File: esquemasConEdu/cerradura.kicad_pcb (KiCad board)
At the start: 2 copper layers, 87.7 x 141.8 mm, 20 parts, among them T1 BC547, T2 BC547

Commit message: corregido distancia limite tracks con borde, pads ampliados y pines EDU con numeros pares
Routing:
- net GND: track 150.6 -> 134.0 mm
- net /kp_c2: track 35.3 -> 38.0 mm
- net /rc522-mosi: track 43.8 -> 46.4 mm
- net +5V: track 334.9 -> 332.4 mm
- net /kp_f2: track 30.0 -> 32.2 mm
- net /rc522-sck: track 57.9 -> 56.6 mm
- net /ssd1306_sda: track 77.9 -> 76.9 mm
- net +12V: track 191.8 -> 191.0 mm
- net /ssd1306_scl: track 76.7 -> 76.0 mm

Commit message: corregido distancia limite tracks con borde, pads ampliados y pines EDU con numeros pares
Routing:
- net +3.3V: track 270.5 -> 271.8 mm
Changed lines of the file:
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@@
 			)
 		)
+		(pad "0" thru_hole circle
+			(at 0 2.54 90)
+			(size 2 2)
+			(drill 0.7)
+			(layers "*.Cu" "*.Mask")
+			(remove_unused_layers no)
+			(pinfunction "~{EN}")
+			(pintype "input")
+		)
+		(pad "0" thru_hole oval
+			(at 12.68 12.7 90)
+			(size 2 2)
+			(drill 0.7)
+			(layers "*.Cu" "*.Mask")
+			(remove_unused_layers no)
+			(pinfunction "~{EN}")
+			(pintype "input")
+		)
+		(pad "0" thru_hole oval
+			(at 12.69 15.24 90)
+			(size 2 2)
+			(drill 0.7)
+			(layers "*.Cu" "*.Mask")
+			(remove_unused_layers no)
+			(pinfunction "~{EN}")
+			(pintype "input")
+		)
+		(pad "0" thru_hole circle
+			(at 12.71 10.16 90)
+			(size 2 2)
+			(drill 0.7)
+			(layers "*.Cu" "*.Mask")
+			(remove_unused_layers no)
+			(pinfunction "~{EN}")
+			(pintype "input")
+		)
 		(pad "1" thru_hole oval
 			(at 0 0 90)
@@
 		(pad "9" thru_hole circle
 			(at 12.7 17.78 90)
-			(size 1.7 1.7)
+			(size 2 2)
 			(drill 0.7)
 			(layers "*.Cu" "*.Mask")
@@
 			)
 		)
+		(pad "0" thru_hole oval
+			(at -2.55 0)
+			(size 2 2)
+			(drill 0.7)
+			(layers "*.Cu" "*.Mask")
+			(remove_unused_layers no)
+			(pinfunction "~{EN}")
+			(pintype "input")
+		)
+		(pad "0" thru_hole circle
+			(at 12.68 5.08)
+			(size 2 2)
+			(drill 0.7)
+			(layers "*.Cu" "*.Mask")
+			(remove_unused_layers no)
+			(pinfunction "~{EN}")
+			(pintype "input")
+		)
 		(pad "1" thru_hole circle
 			(at 12.7 0 180)
@@
 	)
 	(segment
-		(start 114.216 160.784)
-		(end 114.216 122.196159)
+		(start 85.41 167.64)
+		(end 107.36 167.64)
+		(width 1)
+		(layer "B.Cu")
+		(net 1)
+	)
+	(segment
+		(start 73.19 170.26)
+		(end 73.19 165.48)
 		(width 1)
 		(layer "B.Cu")
@@
 	)
 	(segment
+		(start 80.58 162.81)
+		(end 85.41 167.64)
+		(width 1)
+		(layer "B.Cu")
+		(net 1)
+	)
+	(segment
 		(start 99.3925 85.7)
 		(end 101.88 85.7)
@@
 	)
 	(segment
-		(start 114.216 122.196159)
-		(end 112.489841 120.47)
+		(start 107.36 167.64)
+		(end 114.216 160.784)
 		(width 1)
 		(layer "B.Cu")
@@
 	)
 	(segment
-		(start 122.62 85.7)
-		(end 101.88 85.7)
+		(start 112.489841 120.47)
+		(end 109.41 120.47)
 		(width 1)
 		(layer "B.Cu")
@@
 	)
 	(segment
-		(start 79.519 163.819)
-		(end 83.34 167.64)
+		(start 73.19 165.48)
+		(end 75.86 162.81)
 		(width 1)
 		(layer "B.Cu")
@@
 	)
 	(segment
-		(start 64.19 110.15)
-		(end 62.28 112.06)
+		(start 122.62 85.7)
+		(end 101.88 85.7)
 		(width 1)
 		(layer "B.Cu")
@@
 	)
 	(segment
-		(start 107.36 167.64)
-		(end 114.216 160.784)
+		(start 64.19 110.15)
+		(end 62.28 112.06)
 		(width 1)
 		(layer "B.Cu")
@@
 	)
 	(segment
-		(start 73.19 170.26)
-		(end 73.19 166.24)
+		(start 114.216 122.196159)
+		(end 112.489841 120.47)
 		(width 1)
 		(layer "B.Cu")
@@
 	)
 	(segment
-		(start 75.611 163.819)
-		(end 79.519 163.819)
+		(start 114.216 160.784)
+		(end 114.216 122.196159)
 		(width 1)
 		(layer "B.Cu")
@@
 	)
 	(segment
-		(start 137.61 110.11)
-		(end 137.61 100.69)
+		(start 75.86 162.81)
+		(end 80.58 162.81)
 		(width 1)
 		(layer "B.Cu")
@@
 	)
 	(segment
-		(start 112.489841 120.47)
-		(end 109.41 120.47)
+		(start 137.61 110.11)
+		(end 137.61 100.69)
 		(width 1)
 		(layer "B.Cu")
@@
 	)
 	(segment
-		(start 83.34 167.64)
-		(end 107.36 167.64)
-		(width 1)
-		(layer "B.Cu")
-		(net 1)
-	)
-	(segment
-		(start 73.19 166.24)
-		(end 75.611 163.819)
-		(width 1)
-		(layer "B.Cu")
-		(net 1)
-	)
-	(segment
 		(start 74.15 115.22)
 		(end 69.03 115.22)
@@
 	)
 	(segment
-		(start 78.42 166.32)
-		(end 78.42 166.5)
+		(start 80.19 166.32)
+		(end 83.35 169.48)
 		(width 1)
 		(layer "B.Cu")
@@
 	)
 	(segment
-		(start 78.42 166.5)
-		(end 82.18 170.26)
+		(start 78.42 166.32)
+		(end 80.19 166.32)
 		(width 1)
 		(layer "B.Cu")
@@
 	)
 	(segment
-		(start 82.18 170.26)
+		(start 83.35 169.48)
 		(end 83.35 170.26)
 		(width 1)
@@
 	)
 	(segment
-		(start 112.215 123.025)
-		(end 109.3 123.025)
+		(start 112.18 157.45)
+		(end 112.18 123.06)
 		(width 1)
 		(layer "B.Cu")
@@
 	)
 	(segment
-		(start 112.18 123.06)
-		(end 112.215 123.025)
+		(start 103.991 165.639)
+		(end 112.18 157.45)
 		(width 1)
 		(layer "B.Cu")
@@
 	)
 	(segment
-		(start 103.991 165.639)
-		(end 112.18 157.45)
+		(start 76.93 155.87)
+		(end 86.699 165.639)
 		(width 1)
 		(layer "B.Cu")
@@
 	)
 	(segment
-		(start 75.029842 155.87)
-		(end 84.798842 165.639)
+		(start 86.699 165.639)
+		(end 103.991 165.639)
 		(width 1)
 		(layer "B.Cu")
@@
 	(segment
 		(start 69.01 155.87)
-		(end 75.029842 155.87)
+		(end 76.93 155.87)
 		(width 1)
 		(layer "B.Cu")
@@
 	)
 	(segment
-		(start 84.798842 165.639)
-		(end 103.991 165.639)
+		(start 112.18 123.06)
+		(end 112.215 123.025)
 		(width 1)
 		(layer "B.Cu")
@@
 	)
 	(segment
-		(start 112.18 157.45)
-		(end 112.18 123.06)
+		(start 112.215 123.025)
+		(end 109.3 123.025)
 		(width 1)
 		(layer "B.Cu")
@@
 	)
 	(segment
-		(start 70.055949 138.041)
-		(end 71.521 136.575949)
-		(width 1)
-		(layer "B.Cu")
-		(net 21)
-	)
-	(segment
 		(start 66.47 135.55)
-		(end 66.47 136.526949)
-		(width 1)
-		(layer "B.Cu")
-		(net 21)
-	)
-	(segment
-		(start 66.47 136.526949)
-		(end 67.984051 138.041)
+		(end 66.47 136.951213)
 		(width 1)
 		(layer "B.Cu")
@@
 	)
 	(segment
-		(start 71.521 136.575949)
-		(end 74.094051 136.575949)
+		(start 72.629 138.041)
+		(end 77.485 133.185)
 		(width 1)
 		(layer "B.Cu")
@@
 	)
 	(segment
-		(start 74.094051 136.575949)
-		(end 77.485 133.185)
+		(start 66.47 136.951213)
+		(end 67.559787 138.041)
 		(width 1)
 		(layer "B.Cu")
@@
 	)
 	(segment
-		(start 67.984051 138.041)
-		(end 70.055949 138.041)
+		(start 67.559787 138.041)
+		(end 72.629 138.041)
 		(width 1)
 		(layer "B.Cu")
@@
 	)
 	(segment
-		(start 137.61 140.59)
-		(end 131.95 140.59)
+		(start 128.27 136.91)
+		(end 128.27 122.93)
 		(width 1)
 		(layer "B.Cu")
@@
 	)
 	(segment
-		(start 128.27 136.91)
-		(end 128.27 123.42)
+		(start 137.61 140.59)
+		(end 131.95 140.59)
 		(width 1)
 		(layer "B.Cu")
@@
 	)
 	(segment
-		(start 107.835 102.985)
-		(end 106.94 102.985)
+		(start 128.27 122.93)
+		(end 108.325 102.985)
 		(width 1)
 		(layer "B.Cu")
@@
 	)
 	(segment
-		(start 128.27 123.42)
-		(end 107.835 102.985)
+		(start 108.325 102.985)
+		(end 106.94 102.985)
 		(width 1)
 		(layer "B.Cu")

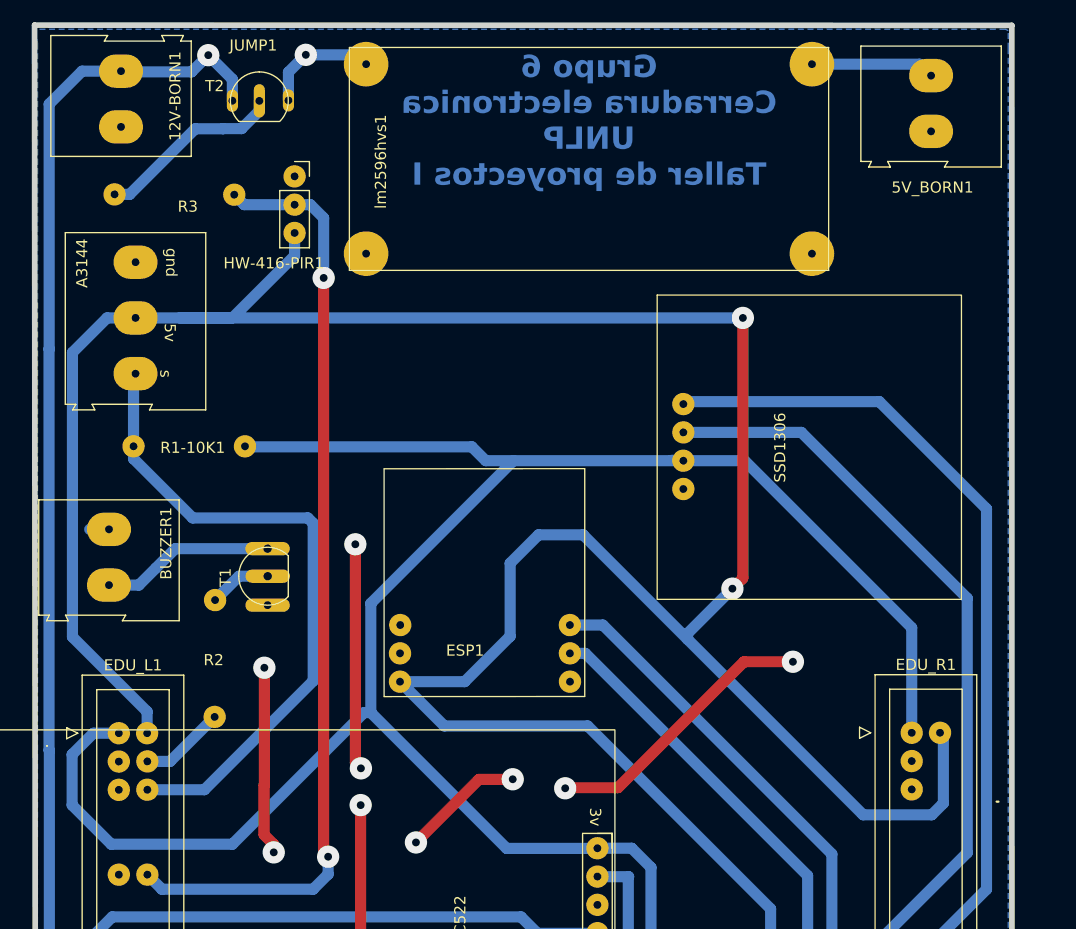
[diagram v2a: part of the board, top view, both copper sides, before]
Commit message: correccion en modulo de deteccion de presencia
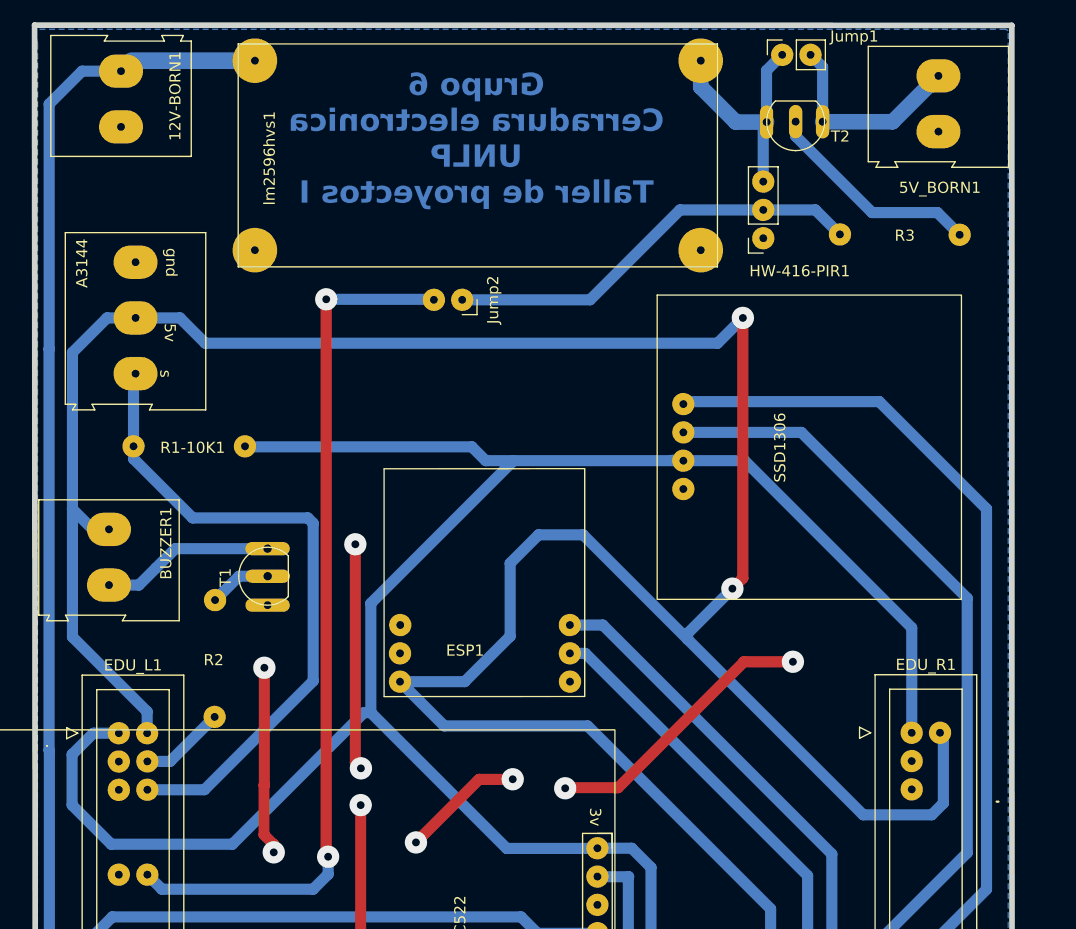
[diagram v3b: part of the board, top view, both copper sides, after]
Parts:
- added Jump1: Jump1, Connector_PinSocket_2.54mm:PinSocket_1x02_P2.54mm_Vertical, F.Cu at (126.0, 49.3)
- added Jump2: Jump2, Connector_PinSocket_2.54mm:PinSocket_1x02_P2.54mm_Vertical, F.Cu at (97.3, 71.3)
- moved R3 65.1 mm to (136.5, 65.5), turned to 0 degrees
- moved T2 50.7 mm to (128.5, 55.3), turned to 180 degrees
- moved HW-416-PIR1 42.4 mm to (124.3, 65.7), turned to 180 degrees
- moved lm2596hvs1 9.98 mm to (98.7, 57.3)
- moved 5V_BORN1 0.66 mm to (140.0, 51.2)
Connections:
- 5V_BORN1 pad 1: +5V-out -> +5V-out-b
- EDU_L1 pad 12: /hw-416-sgn -> /hw-416-sgn-a
- HW-416-PIR1 pad 3: +5V -> +5V-out-a
- T2 pad 1: +12V -> +5V-out-b
- T2 pad 3: +12V -> +5V-out-a
- lm2596hvs1 pad 2: +5V-out -> +5V-out-a
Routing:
- net /hw-416-sgn-a: track 0.00 -> 78.7 mm, vias 0 -> 2
- net /hw-416-sgn: track 85.2 -> 38.1 mm, vias 2 -> 0
- net +5V-out-a: track 0.00 -> 21.6 mm
- net +5V-out-b: track 0.00 -> 18.7 mm
- net +5V-out: track 11.1 -> 0.00 mm
- net +5V: track 332.4 -> 322.0 mm
- net +12V: track 191.0 -> 181.0 mm, vias 2 -> 0
- net Net-(T2-B): track 17.0 -> 19.7 mm
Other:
- board text removed: "JUMP1"
